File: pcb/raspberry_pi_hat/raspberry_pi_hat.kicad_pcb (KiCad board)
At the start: 2 copper layers, 87.5 x 85 mm, 34 parts, among them J1 I2C, J2 IMU, J3 Raspberry_Pi_2_3, J4 PWM, SW1 SW_Push, SW2 SW_Push, SW3 SW_Push

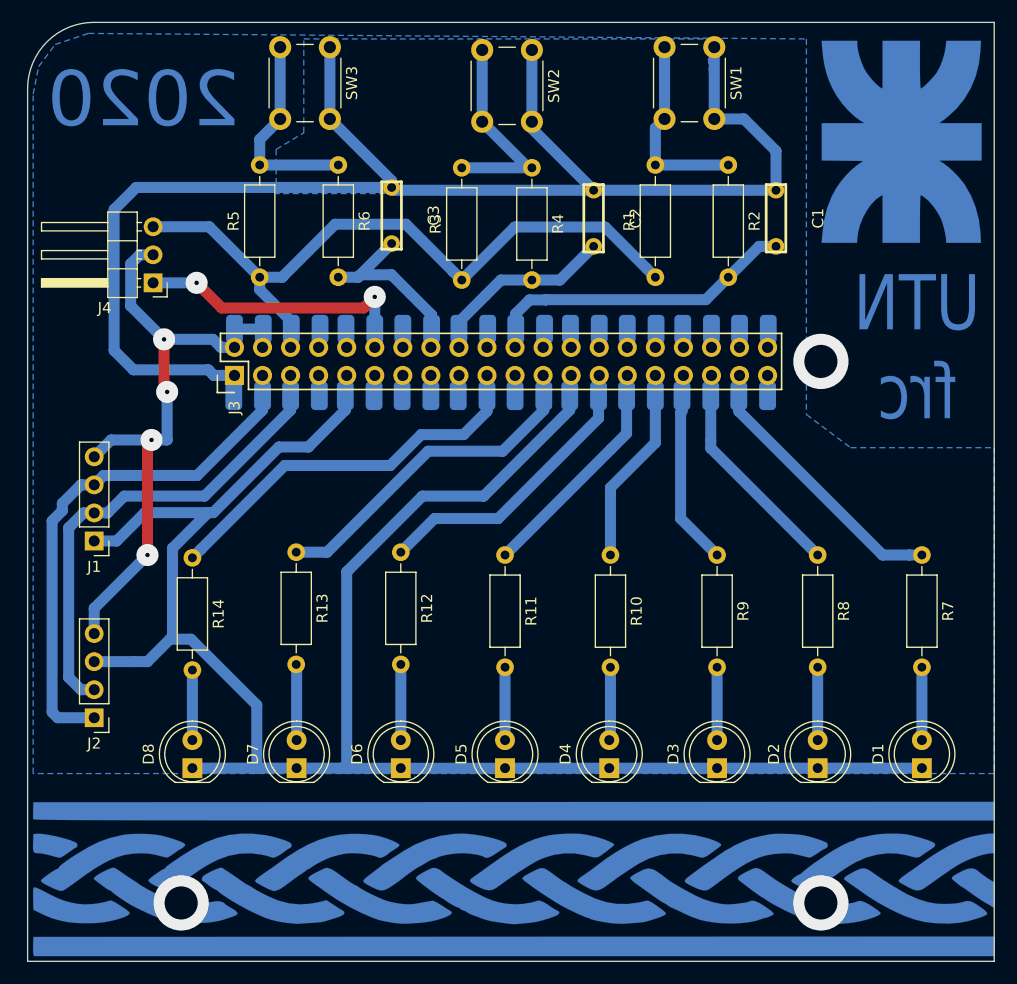
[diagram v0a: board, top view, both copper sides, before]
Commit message: Agrega modificaciones en el tamaño del PCB
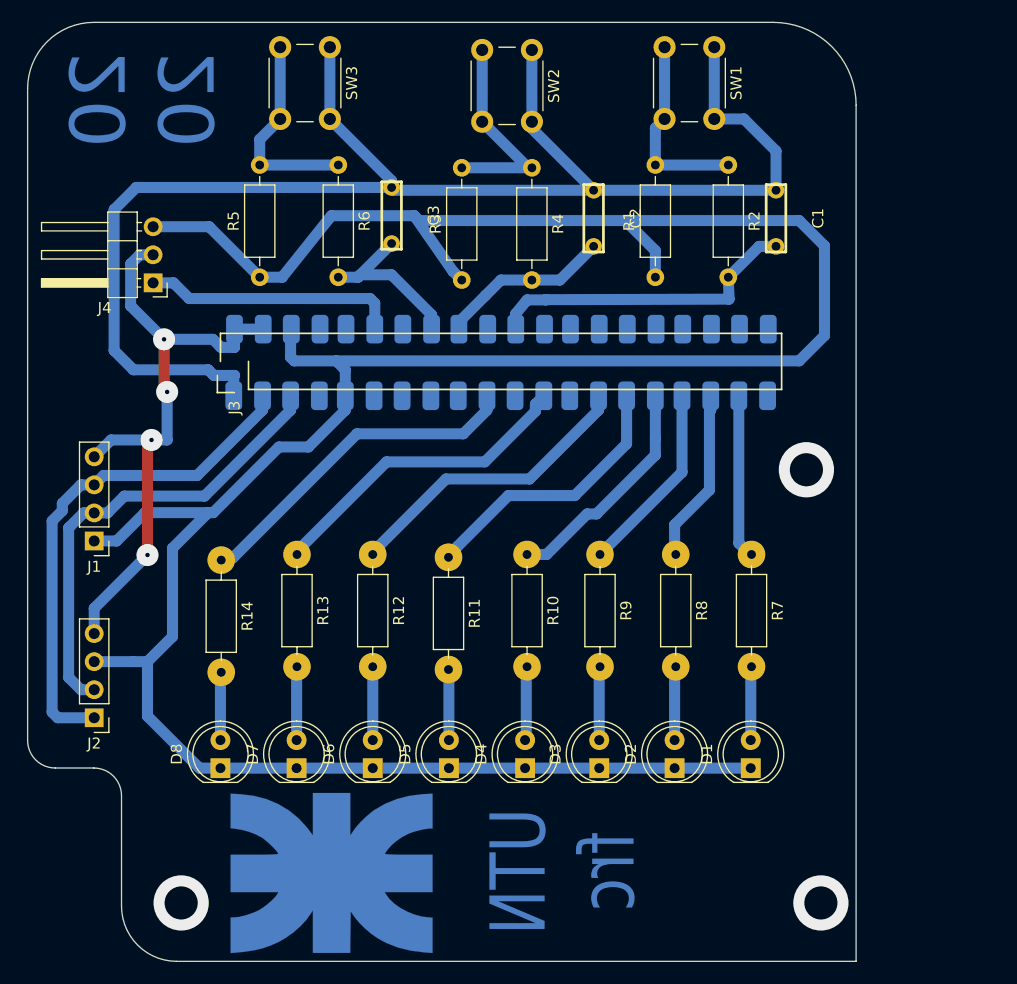
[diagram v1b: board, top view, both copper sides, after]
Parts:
- removed the G*** at (119.0, 122.5)
- R10, R11, R12, R13, R14, R7, R8, R9: footprint Resistor_THT:R_Axial_DIN0207_L6.3mm_D2.5mm_P10.16mm_Horizontal -> Resistor_THT:R_BIG_Axial_DIN0207
- moved G*** 82.3 mm to (103.7, 122.1), turned to 90 degrees
- moved D1 15.5 mm to (140.5, 112.5)
- moved R7 15.4 mm to (140.5, 93.2)
- moved D2 13.0 mm to (133.6, 112.5)
- moved R8 12.8 mm to (133.7, 93.2)
- moved D3 10.7 mm to (126.7, 112.5)
- moved R9 10.6 mm to (126.8, 93.2)
- moved D4 7.62 mm to (120.0, 112.5)
- moved R10 7.55 mm to (120.2, 93.2)
- moved R11 5.12 mm to (113.1, 93.4)
- moved D5 5.08 mm to (113.1, 112.5)
- moved R14 2.62 mm to (92.5, 93.7)
- moved R12 2.55 mm to (106.2, 93.2)
- moved D6 2.54 mm to (106.2, 112.5)
- moved D8 2.54 mm to (92.5, 112.5)
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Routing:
- net /LED_0: track 26.5 -> 15.0 mm
- net GND: track 244.8 -> 255.7 mm
- net /LED_7: track 37.4 -> 31.8 mm
- net /LED_1: track 20.3 -> 15.9 mm
- net /BOTON_1: track 19.0 -> 15.0 mm
- net /LED_6: track 32.3 -> 29.0 mm
- net /BOTON_2: track 18.5 -> 15.6 mm
- net /LED_3: track 17.9 -> 20.7 mm
- net /LED_4: track 22.1 -> 24.7 mm
- net VCC: track 59.2 -> 57.6 mm
- net /BOTON_0: track 27.5 -> 28.8 mm
- net /SDA: track 47.4 -> 46.2 mm
- net /SCL: track 43.3 -> 42.1 mm
- net /PWM_0: track 24.3 -> 23.2 mm, vias 2 -> 0
- net /LED_5: track 28.2 -> 27.2 mm
- removed copper zone on B.Cu, net +3V3
- removed copper zone on B.Cu, net GND
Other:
- board size 87.5 x 85 mm -> 75 x 85 mm
- board text added: "20 20"
- board text removed: "2020"
